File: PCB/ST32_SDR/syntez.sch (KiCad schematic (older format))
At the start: 12 parts, among them U1 SI5351A, Y2 Crystal

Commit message: UI PCB linux 1
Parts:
- R22, R23: footprint (none) -> UI:R_1206_0603
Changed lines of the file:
@@
 LIBS:4ms-ic
 LIBS:Display
-LIBS:switches
-LIBS:cmos4000
+LIBS:Connector
+LIBS:Relay
 LIBS:LCSDR-cache
 EELAYER 25 0
@@
 	3550 1500 3550 2250
 $Comp
-L +3V3 #PWR01
+L +3V3 #PWR06
 U 1 1 5DDEDF62
 P 3550 1500
-F 0 "#PWR01" H 3550 1350 50  0001 C CNN
+F 0 "#PWR06" H 3550 1350 50  0001 C CNN
 F 1 "+3V3" H 3550 1640 50  0000 C CNN
 F 2 "" H 3550 1500 50  0001 C CNN
@@
 	3000 2900 2550 2900
 $Comp
-L GND #PWR02
+L GND #PWR07
 U 1 1 5DDEE4A0
 P 3150 1800
-F 0 "#PWR02" H 3150 1550 50  0001 C CNN
+F 0 "#PWR07" H 3150 1550 50  0001 C CNN
 F 1 "GND" H 3150 1650 50  0001 C CNN
 F 2 "" H 3150 1800 50  0001 C CNN
@@
 $EndComp
 $Comp
-L GND #PWR03
+L GND #PWR08
 U 1 1 5DDEE4E1
 P 5000 2450
-F 0 "#PWR03" H 5000 2200 50  0001 C CNN
+F 0 "#PWR08" H 5000 2200 50  0001 C CNN
 F 1 "GND" H 5000 2300 50  0001 C CNN
 F 2 "" H 5000 2450 50  0001 C CNN
@@
 $EndComp
 $Comp
-L +3V3 #PWR04
+L +3V3 #PWR09
 U 1 1 5DDEE519
 P 5000 2550
-F 0 "#PWR04" H 5000 2400 50  0001 C CNN
+F 0 "#PWR09" H 5000 2400 50  0001 C CNN
 F 1 "+3V3" V 5000 2800 50  0000 C CNN
 F 2 "" H 5000 2550 50  0001 C CNN
@@
 Connection ~ 6100 1100
 $Comp
-L GND #PWR05
+L GND #PWR010
 U 1 1 5DDEEBF2
 P 6100 1400
-F 0 "#PWR05" H 6100 1150 50  0001 C CNN
+F 0 "#PWR010" H 6100 1150 50  0001 C CNN
 F 1 "GND" H 6100 1250 50  0001 C CNN
 F 2 "" H 6100 1400 50  0001 C CNN
@@
 $EndComp
 $Comp
-L GND #PWR06
+L GND #PWR011
 U 1 1 5DDEEC35
 P 6100 2150
-F 0 "#PWR06" H 6100 1900 50  0001 C CNN
+F 0 "#PWR011" H 6100 1900 50  0001 C CNN
 F 1 "GND" H 6100 2000 50  0001 C CNN
 F 2 "" H 6100 2150 50  0001 C CNN
@@
 	6100 2650 6100 2750
 $Comp
-L GND #PWR07
+L GND #PWR012
 U 1 1 5DDEECF7
 P 6100 2950
-F 0 "#PWR07" H 6100 2700 50  0001 C CNN
+F 0 "#PWR012" H 6100 2700 50  0001 C CNN
 F 1 "GND" H 6100 2800 50  0001 C CNN
 F 2 "" H 6100 2950 50  0001 C CNN
@@
 F 0 "R22" V 1750 1050 50  0000 L CNN
 F 1 "56" V 1650 1050 50  0000 L CNN
-F 2 "" H 1550 1050 50  0001 C CNN
+F 2 "UI:R_1206_0603" H 1550 1050 50  0001 C CNN
 F 3 "" H 1550 1050 50  0001 C CNN
 	1    1550 1050
@@
 F 0 "R23" V 1450 1300 50  0000 L CNN
 F 1 "56" V 1350 1300 50  0000 L CNN
-F 2 "" H 1550 1300 50  0001 C CNN
+F 2 "UI:R_1206_0603" H 1550 1300 50  0001 C CNN
 F 3 "" H 1550 1300 50  0001 C CNN
 	1    1550 1300

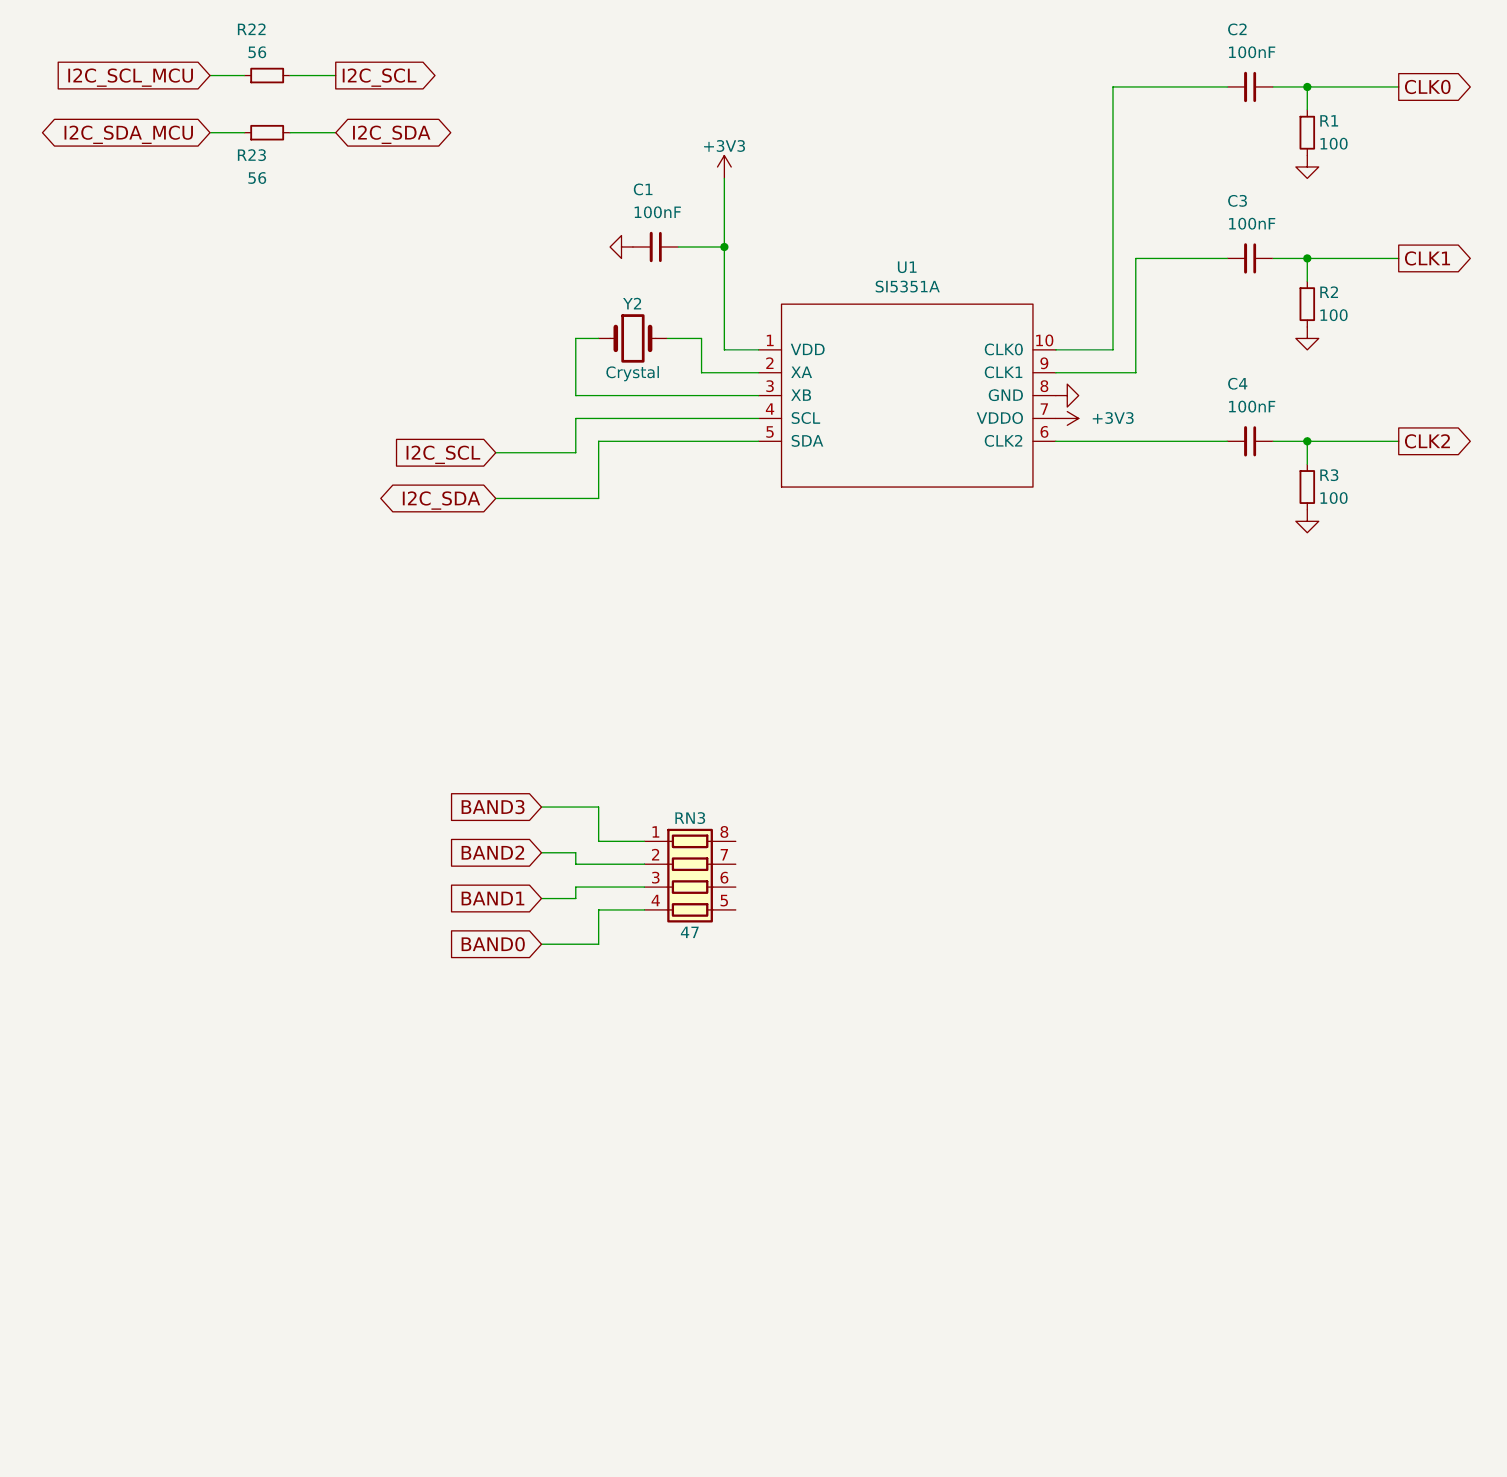
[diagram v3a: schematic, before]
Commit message: PCB Linux 2, update AUDIO_OUT
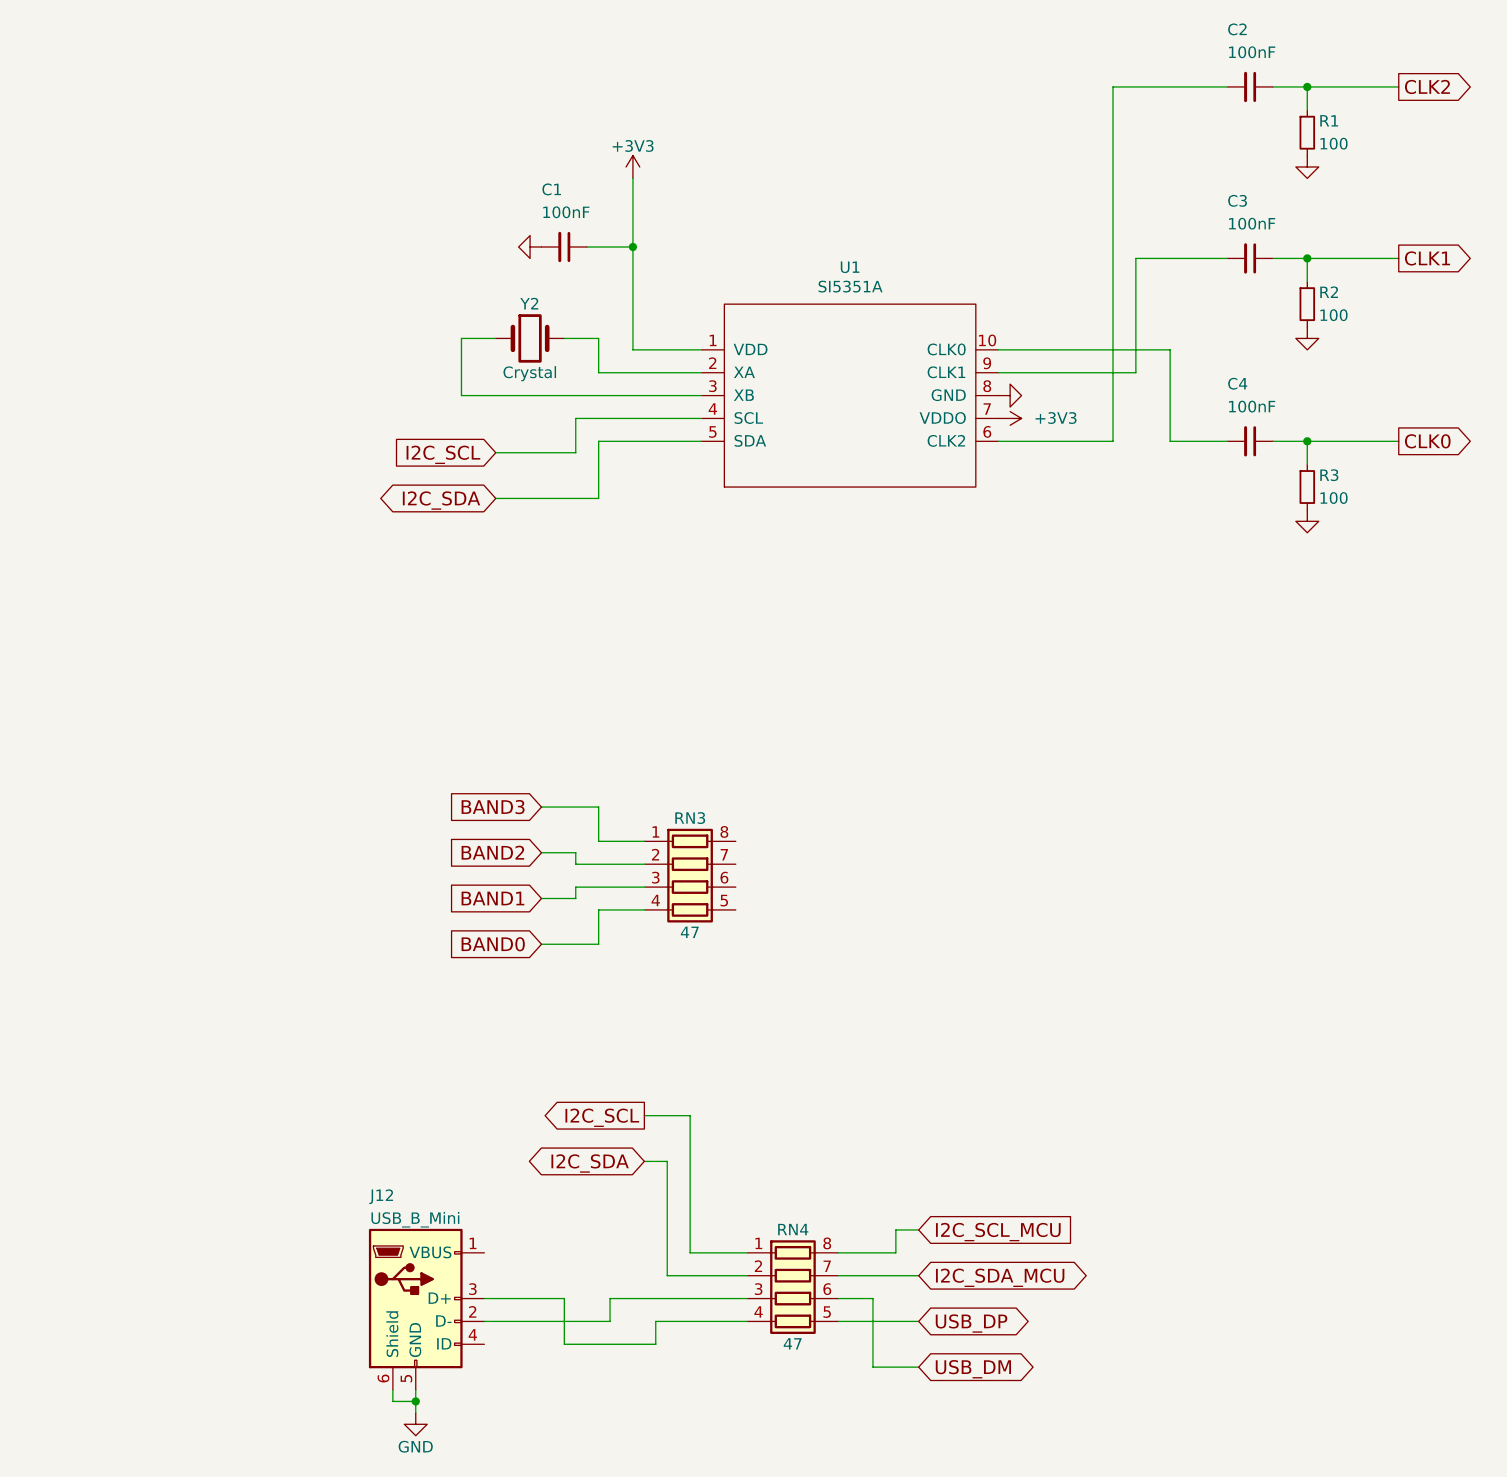
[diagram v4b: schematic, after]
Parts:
- removed R22, R23: 56, UI:R_1206_0603, symbol R_Small
- added J12: USB_B_Mini, Connect:USB_Mini-B, symbol USB_B_Mini
- added RN4: 47, Resistors_SMD:R_Array_Convex_4x0603, symbol R_Pack04
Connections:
- net CLK0: now also C4.1, R3.1; no longer C2.1, R1.1
- net CLK2: now also C2.1, R1.1; no longer C4.1, R3.1
- net GND: now also J12.5 (GND), J12.6 (Shield)
- net I2C_SCL: now also RN4.1 (R1.1)
- net I2C_SCL_MCU: now also RN4.8 (R1.2)
- net I2C_SDA: now also RN4.2 (R2.1)
- net I2C_SDA_MCU: now also RN4.7 (R2.2)
- net at U1.10 (CLK0): now also C4.2; no longer C2.2
- net at U1.6 (CLK2): now also C2.2; no longer C4.2
- new net: J12.2 (D-), RN4.3 (R3.1)
- new net: J12.3 (D+), RN4.4 (R4.1)
- new net USB_DM: RN4.6 (R3.2)
- new net USB_DP: RN4.5 (R4.2)
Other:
- moved on the sheet: C1, U1, Y2
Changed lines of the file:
@@
 LIBS:4ms-ic
 LIBS:Display
-LIBS:switches
-LIBS:cmos4000
+LIBS:Connector
+LIBS:Relay
 LIBS:LCSDR-cache
 EELAYER 25 0
@@
 L SI5351A U1
 U 1 1 5DDEDE1A
-P 4350 2450
-F 0 "U1" H 4350 3010 50  0000 C CNN
-F 1 "SI5351A" H 4350 2925 50  0000 C CNN
-F 2 "Housings_SSOP:MSOP-10_3x3mm_Pitch0.5mm" H 4350 2450 50  0001 C CNN
-F 3 "DOCUMENTATION" H 4370 2310 50  0001 C CNN
-	1    4350 2450
+P 4100 2450
+F 0 "U1" H 4100 3010 50  0000 C CNN
+F 1 "SI5351A" H 4100 2925 50  0000 C CNN
+F 2 "Housings_SSOP:MSOP-10_3x3mm_Pitch0.5mm" H 4100 2450 50  0001 C CNN
+F 3 "DOCUMENTATION" H 4120 2310 50  0001 C CNN
+	1    4100 2450
 	1    0    0    -1
 $EndComp
@@
 L Crystal Y2
 U 1 1 5DDEDE6A
-P 3150 2200
-F 0 "Y2" H 3150 2350 50  0000 C CNN
-F 1 "Crystal" H 3150 2050 50  0000 C CNN
-F 2 "Crystals:Crystal_HC49-U_Vertical" H 3150 2200 50  0001 C CNN
-F 3 "" H 3150 2200 50  0001 C CNN
-	1    3150 2200
-	1    0    0    -1
-$EndComp
-Wire Wire Line
-	3300 2200 3450 2200
-Wire Wire Line
-	3450 2200 3450 2350
-Wire Wire Line
-	3450 2350 3700 2350
-Wire Wire Line
-	3700 2450 2900 2450
-Wire Wire Line
-	2900 2450 2900 2200
-Wire Wire Line
-	2900 2200 3000 2200
-Wire Wire Line
-	3550 2250 3700 2250
-Wire Wire Line
-	3550 1500 3550 2250
+P 2700 2200
+F 0 "Y2" H 2700 2350 50  0000 C CNN
+F 1 "Crystal" H 2700 2050 50  0000 C CNN
+F 2 "Crystals:Crystal_HC49-U_Vertical" H 2700 2200 50  0001 C CNN
+F 3 "" H 2700 2200 50  0001 C CNN
+	1    2700 2200
+	1    0    0    -1
+$EndComp
+Wire Wire Line
+	3000 2350 3450 2350
+Wire Wire Line
+	2400 2450 3450 2450
+Wire Wire Line
+	3150 2250 3450 2250
+Wire Wire Line
+	3150 1500 3150 2250
 $Comp
 L +3V3 #PWR06
 U 1 1 5DDEDF62
-P 3550 1500
-F 0 "#PWR06" H 3550 1350 50  0001 C CNN
-F 1 "+3V3" H 3550 1640 50  0000 C CNN
-F 2 "" H 3550 1500 50  0001 C CNN
-F 3 "" H 3550 1500 50  0001 C CNN
-	1    3550 1500
+P 3150 1500
+F 0 "#PWR06" H 3150 1350 50  0001 C CNN
+F 1 "+3V3" H 3150 1640 50  0000 C CNN
+F 2 "" H 3150 1500 50  0001 C CNN
+F 3 "" H 3150 1500 50  0001 C CNN
+	1    3150 1500
 	1    0    0    -1
 $EndComp
@@
 L C_Small C1
 U 1 1 5DDEDF94
-P 3250 1800
-F 0 "C1" V 3000 1700 50  0000 L CNN
-F 1 "100nF" V 3100 1700 50  0000 L CNN
-F 2 "UI:C_1206_0603" H 3250 1800 50  0001 C CNN
-F 3 "" H 3250 1800 50  0001 C CNN
-	1    3250 1800
-	0    1    1    0
-$EndComp
-Wire Wire Line
-	3350 1800 3550 1800
-Connection ~ 3550 1800
-Wire Wire Line
-	3700 2550 2900 2550
+P 2850 1800
+F 0 "C1" V 2600 1700 50  0000 L CNN
+F 1 "100nF" V 2700 1700 50  0000 L CNN
+F 2 "UI:C_1206_0603" H 2850 1800 50  0001 C CNN
+F 3 "" H 2850 1800 50  0001 C CNN
+	1    2850 1800
+	0    1    1    0
+$EndComp
+Wire Wire Line
+	2950 1800 3150 1800
+Connection ~ 3150 1800
+Wire Wire Line
+	3450 2550 2900 2550
 Wire Wire Line
 	2900 2550 2900 2700
@@
 	2900 2700 2550 2700
 Wire Wire Line
-	3700 2650 3000 2650
+	3450 2650 3000 2650
 Wire Wire Line
 	3000 2650 3000 2900
@@
 L GND #PWR07
 U 1 1 5DDEE4A0
-P 3150 1800
-F 0 "#PWR07" H 3150 1550 50  0001 C CNN
-F 1 "GND" H 3150 1650 50  0001 C CNN
-F 2 "" H 3150 1800 50  0001 C CNN
-F 3 "" H 3150 1800 50  0001 C CNN
-	1    3150 1800
+P 2750 1800
+F 0 "#PWR07" H 2750 1550 50  0001 C CNN
+F 1 "GND" H 2750 1650 50  0001 C CNN
+F 2 "" H 2750 1800 50  0001 C CNN
+F 3 "" H 2750 1800 50  0001 C CNN
+	1    2750 1800
 	0    1    1    0
 $EndComp
@@
 L GND #PWR08
 U 1 1 5DDEE4E1
-P 5000 2450
-F 0 "#PWR08" H 5000 2200 50  0001 C CNN
-F 1 "GND" H 5000 2300 50  0001 C CNN
-F 2 "" H 5000 2450 50  0001 C CNN
-F 3 "" H 5000 2450 50  0001 C CNN
-	1    5000 2450
+P 4750 2450
+F 0 "#PWR08" H 4750 2200 50  0001 C CNN
+F 1 "GND" H 4750 2300 50  0001 C CNN
+F 2 "" H 4750 2450 50  0001 C CNN
+F 3 "" H 4750 2450 50  0001 C CNN
+	1    4750 2450
 	0    -1   -1   0
 $EndComp
@@
 L +3V3 #PWR09
 U 1 1 5DDEE519
-P 5000 2550
-F 0 "#PWR09" H 5000 2400 50  0001 C CNN
-F 1 "+3V3" V 5000 2800 50  0000 C CNN
-F 2 "" H 5000 2550 50  0001 C CNN
-F 3 "" H 5000 2550 50  0001 C CNN
-	1    5000 2550
-	0    1    1    0
-$EndComp
-Wire Wire Line
-	5250 2250 5000 2250
-Wire Wire Line
-	5250 1100 5250 2250
-Wire Wire Line
-	5000 2350 5350 2350
+P 4750 2550
+F 0 "#PWR09" H 4750 2400 50  0001 C CNN
+F 1 "+3V3" V 4750 2800 50  0000 C CNN
+F 2 "" H 4750 2550 50  0001 C CNN
+F 3 "" H 4750 2550 50  0001 C CNN
+	1    4750 2550
+	0    1    1    0
+$EndComp
+Wire Wire Line
+	4750 2350 5350 2350
 Wire Wire Line
 	5350 2350 5350 1850
 Wire Wire Line
 	5350 1850 5750 1850
-Wire Wire Line
-	5000 2650 5750 2650
 $Comp
 L C_Small C4
@@
 	6100 1850 6100 1950
 Text GLabel 6500 1100 2    60   Output ~ 0
-CLK0
+CLK2
 Connection ~ 6100 1100
 $Comp
@@
 Connection ~ 6100 1850
 Text GLabel 6500 2650 2    60   Output ~ 0
-CLK2
+CLK0
 Connection ~ 6100 2650
 $Comp
@@
 Wire Wire Line
 	3000 4700 3200 4700
-Text GLabel 1300 1050 0    60   Input ~ 0
+Text GLabel 4400 6100 2    60   Input ~ 0
 I2C_SCL_MCU
-Text GLabel 1300 1300 0    60   BiDi ~ 0
+Text GLabel 4400 6300 2    60   BiDi ~ 0
 I2C_SDA_MCU
-$Comp
-L R_Small R22
-U 1 1 5DE23CAB
-P 1550 1050
-F 0 "R22" V 1750 1050 50  0000 L CNN
-F 1 "56" V 1650 1050 50  0000 L CNN
-F 2 "UI:R_1206_0603" H 1550 1050 50  0001 C CNN
-F 3 "" H 1550 1050 50  0001 C CNN
-	1    1550 1050
-	0    -1   -1   0
-$EndComp
-$Comp
-L R_Small R23
-U 1 1 5DE23D38
-P 1550 1300
-F 0 "R23" V 1450 1300 50  0000 L CNN
-F 1 "56" V 1350 1300 50  0000 L CNN
-F 2 "UI:R_1206_0603" H 1550 1300 50  0001 C CNN
-F 3 "" H 1550 1300 50  0001 C CNN
-	1    1550 1300
-	0    -1   -1   0
-$EndComp
-Text GLabel 1850 1050 2    60   Output ~ 0
+Text GLabel 3200 5600 0    60   Output ~ 0
 I2C_SCL
-Wire Wire Line
-	1450 1050 1300 1050
-Wire Wire Line
-	1650 1050 1850 1050
-Text GLabel 1850 1300 2    60   BiDi ~ 0
+Text GLabel 3200 5800 0    60   BiDi ~ 0
 I2C_SDA
-Wire Wire Line
-	1850 1300 1650 1300
-Wire Wire Line
-	1450 1300 1300 1300
+$Comp
+L USB_B_Mini J12
+U 1 1 5DE4C0D6
+P 2200 6400
+F 0 "J12" H 2000 6850 50  0000 L CNN
+F 1 "USB_B_Mini" H 2000 6750 50  0000 L CNN
+F 2 "Connect:USB_Mini-B" H 2350 6350 50  0001 C CNN
+F 3 "" H 2350 6350 50  0001 C CNN
+	1    2200 6400
+	1    0    0    -1
+$EndComp
+Wire Wire Line
+	4200 6400 4200 6700
+Wire Wire Line
+	4200 6700 4400 6700
+Text GLabel 4400 6700 2    60   BiDi ~ 0
+USB_DM
+Text GLabel 4400 6500 2    60   BiDi ~ 0
+USB_DP
+$Comp
+L GND #PWR013
+U 1 1 5DE4C0F5
+P 2200 6900
+F 0 "#PWR013" H 2200 6650 50  0001 C CNN
+F 1 "GND" H 2200 6750 50  0000 C CNN
+F 2 "" H 2200 6900 50  0001 C CNN
+F 3 "" H 2200 6900 50  0001 C CNN
+	1    2200 6900
+	1    0    0    -1
+$EndComp
+$Comp
+L R_Pack04 RN4
+U 1 1 5DE4C1DE
+P 3850 6400
+F 0 "RN4" V 3550 6400 50  0000 C CNN
+F 1 "47" V 4050 6400 50  0000 C CNN
+F 2 "Resistors_SMD:R_Array_Convex_4x0603" V 4125 6400 50  0001 C CNN
+F 3 "" H 3850 6400 50  0001 C CNN
+	1    3850 6400
+	0    1    1    0
+$EndComp
+Wire Wire Line
+	4050 6500 4400 6500
+Wire Wire Line
+	4050 6300 4400 6300
+Wire Wire Line
+	3200 5800 3300 5800
+Wire Wire Line
+	3300 5800 3300 6300
+Wire Wire Line
+	3300 6300 3650 6300
+Wire Wire Line
+	2200 6800 2200 6900
+Wire Wire Line
+	2100 6800 2100 6850
+Wire Wire Line
+	2100 6850 2200 6850
+Connection ~ 2200 6850
+Wire Wire Line
+	3200 5600 3400 5600
+Wire Wire Line
+	3400 5600 3400 6200
+Wire Wire Line
+	3400 6200 3650 6200
+Wire Wire Line
+	4400 6100 4300 6100
+Wire Wire Line
+	4300 6100 4300 6200
+Wire Wire Line
+	4300 6200 4050 6200
+Wire Wire Line
+	4050 6400 4200 6400
+Wire Wire Line
+	3650 6400 3050 6400
+Wire Wire Line
+	3050 6400 3050 6500
+Wire Wire Line
+	3050 6500 2500 6500
+Wire Wire Line
+	2500 6400 2850 6400
+Wire Wire Line
+	2850 6400 2850 6600
+Wire Wire Line
+	2850 6600 3250 6600
+Wire Wire Line
+	3250 6600 3250 6500
+Wire Wire Line
+	3250 6500 3650 6500
+Wire Wire Line
+	4750 2250 5500 2250
+Wire Wire Line
+	5500 2250 5500 2650
+Wire Wire Line
+	5500 2650 5750 2650
+Wire Wire Line
+	4750 2650 5250 2650
+Wire Wire Line
+	5250 2650 5250 1100
+Wire Wire Line
+	2400 2450 2400 2200
+Wire Wire Line
+	2400 2200 2550 2200
+Wire Wire Line
+	2850 2200 3000 2200
+Wire Wire Line
+	3000 2200 3000 2350
 $EndSCHEMATC
